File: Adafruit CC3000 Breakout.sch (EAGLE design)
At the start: 30 parts, among them IC1 ATmega1284P, U1 CC3000MOD, X1 2500AT44M0400E

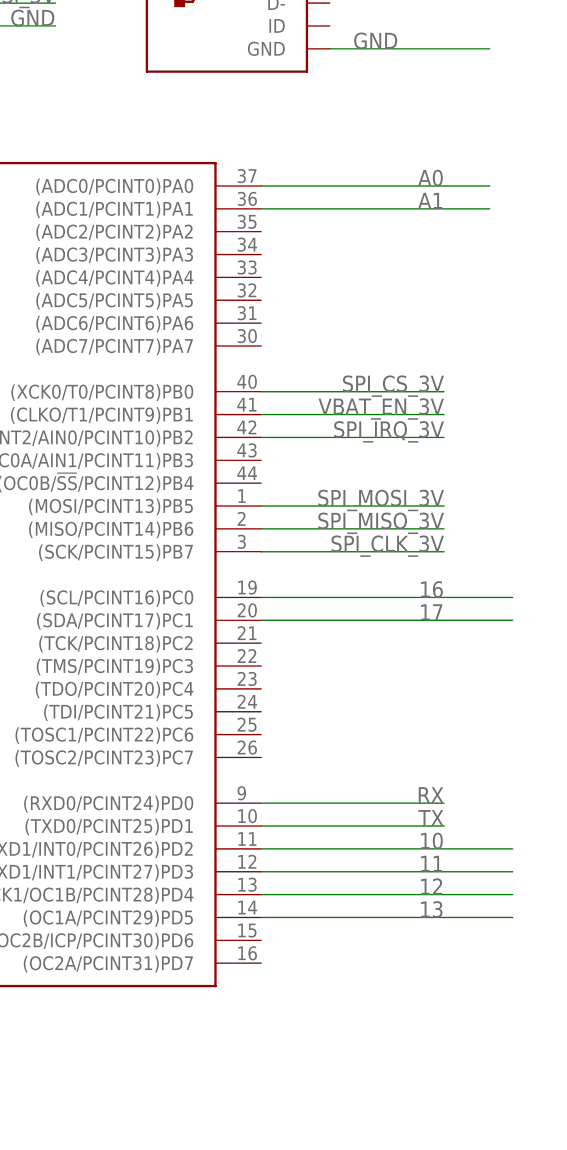
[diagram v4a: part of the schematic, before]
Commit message: Breakout some microcontroller pins.
Partly un-route the board.
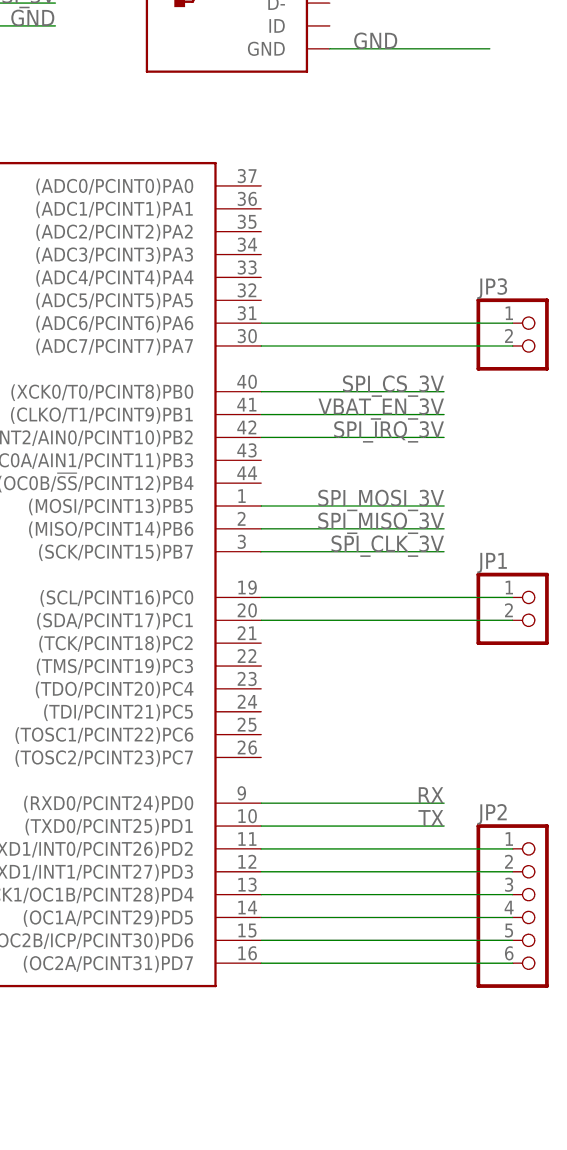
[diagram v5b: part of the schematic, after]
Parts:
- added JP1, JP3: (no value), pinhead:PINHD-1X2
- added JP2: (no value), pinhead:PINHD-1X6
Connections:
- removed net 10: IC1.(RXD1/INT0/PCINT26)PD2
- removed net 11: IC1.(TXD1/INT1/PCINT27)PD3
- removed net 12: IC1.(XCK1/OC1B/PCINT28)PD4
- removed net 13: IC1.(OC1A/PCINT29)PD5
- removed net 16: IC1.(SCL/PCINT16)PC0
- removed net 17: IC1.(SDA/PCINT17)PC1
- removed net A0: IC1.(ADC0/PCINT0)PA0
- removed net A1: IC1.(ADC1/PCINT1)PA1
- new net N$11: IC1.(RXD1/INT0/PCINT26)PD2, JP2.1
- new net N$12: IC1.(TXD1/INT1/PCINT27)PD3, JP2.2
- new net N$13: IC1.(XCK1/OC1B/PCINT28)PD4, JP2.3
- new net N$14: IC1.(OC1A/PCINT29)PD5, JP2.4
- new net N$15: IC1.(OC2B/ICP/PCINT30)PD6, JP2.5
- new net N$16: IC1.(OC2A/PCINT31)PD7, JP2.6
- new net N$17: IC1.(ADC6/PCINT6)PA6, JP3.1
- new net N$18: IC1.(ADC7/PCINT7)PA7, JP3.2
- new net N$5: IC1.(SCL/PCINT16)PC0, JP1.1
- new net N$9: IC1.(SDA/PCINT17)PC1, JP1.2
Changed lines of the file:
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@@
 <part name="CN1" library="Net Widget" deviceset="USB" device="PWR"/>
 <part name="C11" library="rcl" deviceset="C-EU" device="C1206" value="0.1uF"/>
+<part name="JP1" library="pinhead" deviceset="PINHD-1X2" device=""/>
+<part name="JP2" library="pinhead" deviceset="PINHD-1X6" device=""/>
+<part name="JP3" library="pinhead" deviceset="PINHD-1X2" device=""/>
 </parts>
 <sheets>
@@
 <instance part="CN1" gate="G$1" x="220.98" y="160.02"/>
 <instance part="C11" gate="G$1" x="152.4" y="99.06"/>
+<instance part="JP1" gate="G$1" x="254" y="91.44"/>
+<instance part="JP2" gate="A" x="254" y="58.42"/>
+<instance part="JP3" gate="G$1" x="254" y="121.92"/>
 </instances>
 <busses>
@@
 </segment>
 </net>
-<net name="A1" class="0">
-<segment>
-<pinref part="IC1" gate="G$1" pin="(ADC1/PCINT1)PA1"/>
-<wire x1="223.52" y1="137.16" x2="248.92" y2="137.16" width="0.1524" layer="91"/>
-<label x="243.84" y="137.16" size="1.778" layer="95" rot="MR0"/>
-</segment>
-</net>
-<net name="A0" class="0">
-<segment>
-<pinref part="IC1" gate="G$1" pin="(ADC0/PCINT0)PA0"/>
-<wire x1="223.52" y1="139.7" x2="248.92" y2="139.7" width="0.1524" layer="91"/>
-<label x="243.84" y="139.7" size="1.778" layer="95" rot="MR0"/>
-</segment>
-</net>
 <net name="DTR" class="0">
 <segment>
@@
 </segment>
 </net>
-<net name="10" class="0">
+<net name="N$5" class="0">
+<segment>
+<pinref part="IC1" gate="G$1" pin="(SCL/PCINT16)PC0"/>
+<pinref part="JP1" gate="G$1" pin="1"/>
+<wire x1="251.46" y1="93.98" x2="223.52" y2="93.98" width="0.1524" layer="91"/>
+</segment>
+</net>
+<net name="N$9" class="0">
+<segment>
+<pinref part="IC1" gate="G$1" pin="(SDA/PCINT17)PC1"/>
+<pinref part="JP1" gate="G$1" pin="2"/>
+<wire x1="251.46" y1="91.44" x2="223.52" y2="91.44" width="0.1524" layer="91"/>
+</segment>
+</net>
+<net name="N$11" class="0">
 <segment>
 <pinref part="IC1" gate="G$1" pin="(RXD1/INT0/PCINT26)PD2"/>
+<pinref part="JP2" gate="A" pin="1"/>
 <wire x1="251.46" y1="66.04" x2="223.52" y2="66.04" width="0.1524" layer="91"/>
-<label x="243.84" y="66.04" size="1.778" layer="95" rot="MR0"/>
-</segment>
-</net>
-<net name="11" class="0">
+</segment>
+</net>
+<net name="N$12" class="0">
 <segment>
 <pinref part="IC1" gate="G$1" pin="(TXD1/INT1/PCINT27)PD3"/>
+<pinref part="JP2" gate="A" pin="2"/>
 <wire x1="251.46" y1="63.5" x2="223.52" y2="63.5" width="0.1524" layer="91"/>
-<label x="243.84" y="63.5" size="1.778" layer="95" rot="MR0"/>
-</segment>
-</net>
-<net name="12" class="0">
+</segment>
+</net>
+<net name="N$13" class="0">
 <segment>
 <pinref part="IC1" gate="G$1" pin="(XCK1/OC1B/PCINT28)PD4"/>
+<pinref part="JP2" gate="A" pin="3"/>
 <wire x1="251.46" y1="60.96" x2="223.52" y2="60.96" width="0.1524" layer="91"/>
-<label x="243.84" y="60.96" size="1.778" layer="95" rot="MR0"/>
-</segment>
-</net>
-<net name="13" class="0">
+</segment>
+</net>
+<net name="N$14" class="0">
 <segment>
 <pinref part="IC1" gate="G$1" pin="(OC1A/PCINT29)PD5"/>
+<pinref part="JP2" gate="A" pin="4"/>
 <wire x1="251.46" y1="58.42" x2="223.52" y2="58.42" width="0.1524" layer="91"/>
-<label x="243.84" y="58.42" size="1.778" layer="95" rot="MR0"/>
-</segment>
-</net>
-<net name="16" class="0">
-<segment>
-<pinref part="IC1" gate="G$1" pin="(SCL/PCINT16)PC0"/>
-<wire x1="251.46" y1="93.98" x2="223.52" y2="93.98" width="0.1524" layer="91"/>
-<label x="243.84" y="93.98" size="1.778" layer="95" rot="MR0"/>
-</segment>
-</net>
-<net name="17" class="0">
-<segment>
-<pinref part="IC1" gate="G$1" pin="(SDA/PCINT17)PC1"/>
-<wire x1="251.46" y1="91.44" x2="223.52" y2="91.44" width="0.1524" layer="91"/>
-<label x="243.84" y="91.44" size="1.778" layer="95" rot="MR0"/>
-</segment>
-</net>
+</segment>
+</net>
+<net name="N$15" class="0">
+<segment>
+<pinref part="IC1" gate="G$1" pin="(OC2B/ICP/PCINT30)PD6"/>
+<pinref part="JP2" gate="A" pin="5"/>
+<wire x1="251.46" y1="55.88" x2="223.52" y2="55.88" width="0.1524" layer="91"/>
+</segment>
+</net>
+<net name="N$16" class="0">
+<segment>
+<pinref part="IC1" gate="G$1" pin="(OC2A/PCINT31)PD7"/>
+<pinref part="JP2" gate="A" pin="6"/>
+<wire x1="251.46" y1="53.34" x2="223.52" y2="53.34" width="0.1524" layer="91"/>
+</segment>
+</net>
+<net name="N$17" class="0">
+<segment>
+<pinref part="IC1" gate="G$1" pin="(ADC6/PCINT6)PA6"/>
+<pinref part="JP3" gate="G$1" pin="1"/>
+<wire x1="251.46" y1="124.46" x2="223.52" y2="124.46" width="0.1524" layer="91"/>
+</segment>
+</net>
+<net name="N$18" class="0">
+<segment>
+<pinref part="IC1" gate="G$1" pin="(ADC7/PCINT7)PA7"/>
+<pinref part="JP3" gate="G$1" pin="2"/>
+<wire x1="251.46" y1="121.92" x2="223.52" y2="121.92" width="0.1524" layer="91"/>
+</segment>
+</net>

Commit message: Breakout power and ground. Align to inch grid.
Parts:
- added JP4: (no value), pinhead:PINHD-1X2
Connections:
- net GND: now also JP4.2
- net VBAT: now also JP4.1
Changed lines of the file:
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@@
 <part name="JP2" library="pinhead" deviceset="PINHD-1X6" device=""/>
 <part name="JP3" library="pinhead" deviceset="PINHD-1X2" device=""/>
+<part name="JP4" library="pinhead" deviceset="PINHD-1X2" device=""/>
 </parts>
 <sheets>
@@
 <instance part="JP2" gate="A" x="254" y="58.42"/>
 <instance part="JP3" gate="G$1" x="254" y="121.92"/>
+<instance part="JP4" gate="G$1" x="254" y="137.16"/>
 </instances>
 <busses>
@@
 <label x="149.86" y="83.82" size="1.778" layer="95"/>
 </segment>
+<segment>
+<pinref part="JP4" gate="G$1" pin="2"/>
+<wire x1="251.46" y1="137.16" x2="238.76" y2="137.16" width="0.1524" layer="91"/>
+<label x="238.76" y="137.16" size="1.778" layer="95"/>
+</segment>
 </net>
 <net name="N$3" class="0">
@@
 <label x="200.66" y="162.56" size="1.778" layer="95" rot="MR0"/>
 </segment>
-</net>
+<segment>
+<pinref part="JP4" gate="G$1" pin="1"/>
+<wire x1="251.46" y1="139.7" x2="238.76" y2="139.7" width="0.1524" layer="91"/>
+<label x="238.76" y="139.7" size="1.778" layer="95"/>
+</segment>
+</net>

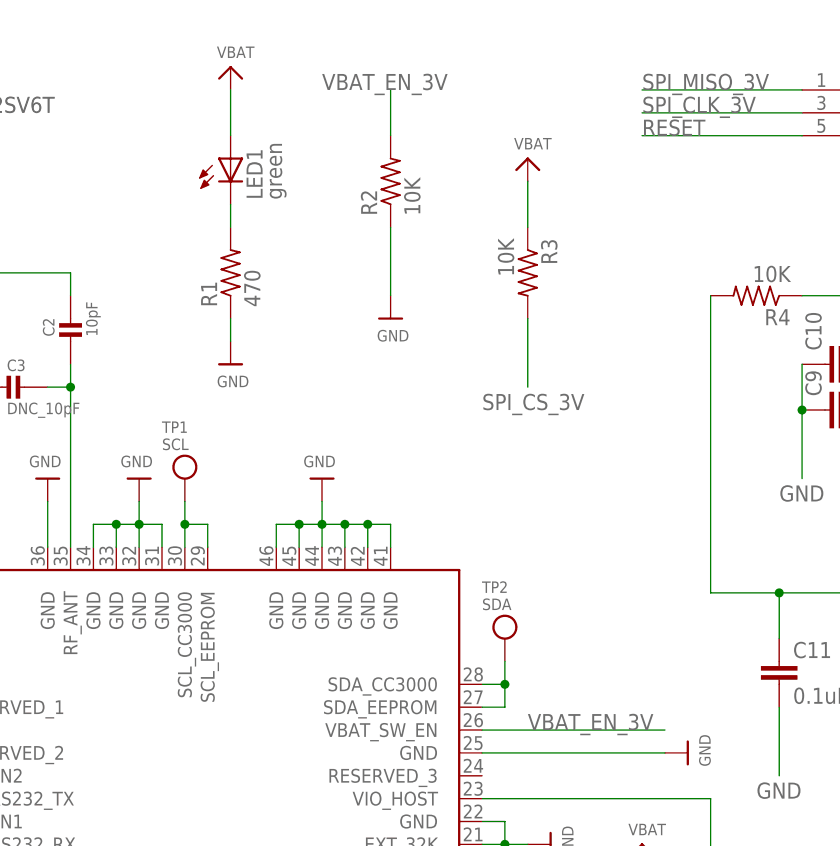
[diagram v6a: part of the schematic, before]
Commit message: Put CC3000 I2C pins on 0.1" pins.
Instead of test points.
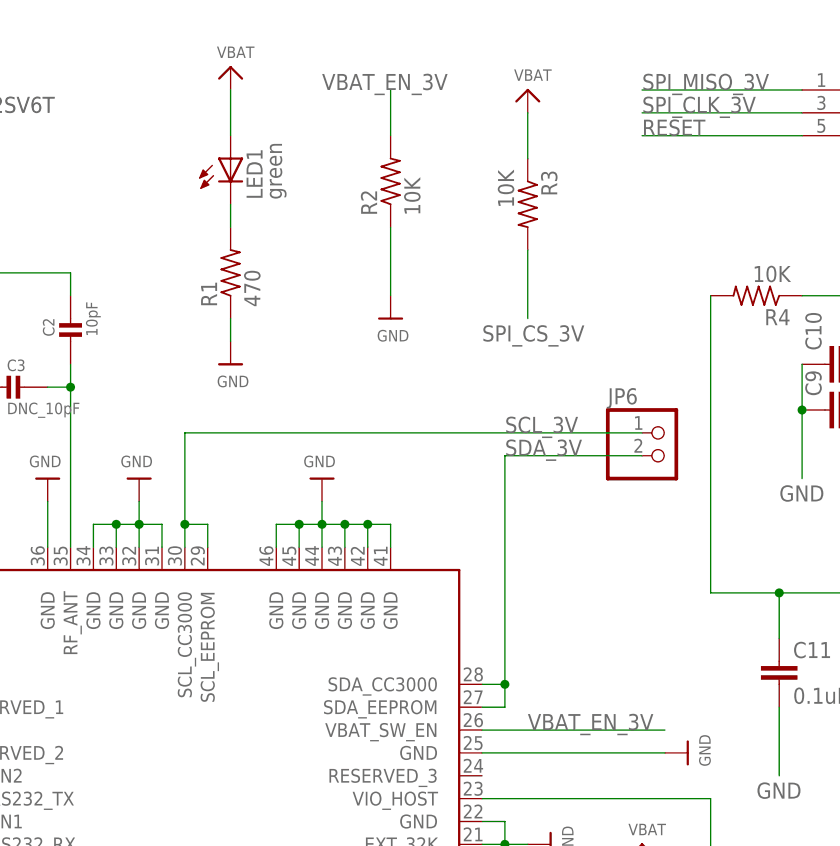
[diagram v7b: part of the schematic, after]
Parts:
- removed TP1: SCL, microbuilder:TESTPOINTPAD1MM
- removed TP2: SDA, microbuilder:TESTPOINTPAD1MM
- added JP6: (no value), pinhead:PINHD-1X2
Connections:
- net SCL_3V: now also JP6.1; no longer TP1.P$1
- net SDA_3V: now also JP6.2; no longer TP2.P$1
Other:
- moved on the sheet: R3
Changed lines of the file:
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@@
 <part name="U$29" library="microbuilder" deviceset="GND" device=""/>
 <part name="U$30" library="microbuilder" deviceset="GND" device=""/>
-<part name="TP1" library="microbuilder" deviceset="TESTPOINT" device="PAD1MM" value="SCL"/>
-<part name="TP2" library="microbuilder" deviceset="TESTPOINT" device="PAD1MM" value="SDA"/>
 <part name="R2" library="rcl" deviceset="R-US_" device="R1206" value="10K"/>
 <part name="U$14" library="microbuilder" deviceset="GND" device=""/>
@@
 <part name="JP3" library="pinhead" deviceset="PINHD-1X2" device=""/>
 <part name="JP4" library="pinhead" deviceset="PINHD-1X2" device=""/>
+<part name="JP6" library="pinhead" deviceset="PINHD-1X2" device=""/>
 </parts>
 <sheets>
@@
 <instance part="U$29" gate="G$1" x="45.72" y="15.24"/>
 <instance part="U$30" gate="G$1" x="33.02" y="15.24"/>
-<instance part="TP1" gate="G$1" x="86.36" y="116.84"/>
-<instance part="TP2" gate="G$1" x="121.92" y="99.06"/>
 <instance part="R2" gate="G$1" x="109.22" y="152.4" rot="R90"/>
 <instance part="U$14" gate="G$1" x="109.22" y="137.16"/>
-<instance part="R3" gate="G$1" x="124.46" y="142.24" rot="R270"/>
-<instance part="U$22" gate="G$1" x="124.46" y="154.94"/>
+<instance part="R3" gate="G$1" x="124.46" y="149.86" rot="R270"/>
+<instance part="U$22" gate="G$1" x="124.46" y="162.56"/>
 <instance part="U$35" gate="G$1" x="55.88" y="129.54"/>
 <instance part="LED1" gate="G$1" x="91.44" y="154.94"/>
@@
 <instance part="JP3" gate="G$1" x="254" y="121.92"/>
 <instance part="JP4" gate="G$1" x="254" y="137.16"/>
+<instance part="JP6" gate="G$1" x="139.7" y="121.92"/>
 </instances>
 <busses>
@@
 <pinref part="U1" gate="G$1" pin="SCL_CC3000"/>
 <wire x1="86.36" y1="111.76" x2="86.36" y2="114.3" width="0.1524" layer="91"/>
-<wire x1="86.36" y1="114.3" x2="86.36" y2="116.84" width="0.1524" layer="91"/>
 <pinref part="U1" gate="G$1" pin="SCL_EEPROM"/>
 <wire x1="88.9" y1="111.76" x2="88.9" y2="114.3" width="0.1524" layer="91"/>
 <wire x1="88.9" y1="114.3" x2="86.36" y2="114.3" width="0.1524" layer="91"/>
 <junction x="86.36" y="114.3"/>
-<pinref part="TP1" gate="G$1" pin="P$1"/>
+<wire x1="86.36" y1="114.3" x2="86.36" y2="124.46" width="0.1524" layer="91"/>
+<wire x1="86.36" y1="124.46" x2="137.16" y2="124.46" width="0.1524" layer="91"/>
+<pinref part="JP6" gate="G$1" pin="1"/>
+<label x="121.92" y="124.46" size="1.778" layer="95"/>
 </segment>
 </net>
@@
 <wire x1="119.38" y1="96.52" x2="121.92" y2="96.52" width="0.1524" layer="91"/>
 <pinref part="U1" gate="G$1" pin="SDA_EEPROM"/>
-<wire x1="121.92" y1="96.52" x2="121.92" y2="99.06" width="0.1524" layer="91"/>
 <wire x1="119.38" y1="93.98" x2="121.92" y2="93.98" width="0.1524" layer="91"/>
 <wire x1="121.92" y1="93.98" x2="121.92" y2="96.52" width="0.1524" layer="91"/>
 <junction x="121.92" y="96.52"/>
-<pinref part="TP2" gate="G$1" pin="P$1"/>
+<wire x1="121.92" y1="96.52" x2="121.92" y2="121.92" width="0.1524" layer="91"/>
+<wire x1="121.92" y1="121.92" x2="137.16" y2="121.92" width="0.1524" layer="91"/>
+<pinref part="JP6" gate="G$1" pin="2"/>
+<label x="121.92" y="121.92" size="1.778" layer="95"/>
 </segment>
 </net>
@@
 <pinref part="R3" gate="G$1" pin="1"/>
 <pinref part="U$22" gate="G$1" pin="VBAT"/>
-<wire x1="124.46" y1="147.32" x2="124.46" y2="152.4" width="0.1524" layer="91"/>
+<wire x1="124.46" y1="154.94" x2="124.46" y2="160.02" width="0.1524" layer="91"/>
 </segment>
 <segment>
@@
 </segment>
 <segment>
-<wire x1="124.46" y1="129.54" x2="124.46" y2="137.16" width="0.1524" layer="91"/>
-<label x="119.38" y="127" size="1.778" layer="95"/>
+<wire x1="124.46" y1="137.16" x2="124.46" y2="144.78" width="0.1524" layer="91"/>
+<label x="119.38" y="134.62" size="1.778" layer="95"/>
 <pinref part="R3" gate="G$1" pin="2"/>
 </segment>
